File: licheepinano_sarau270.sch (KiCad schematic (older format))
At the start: 0 parts

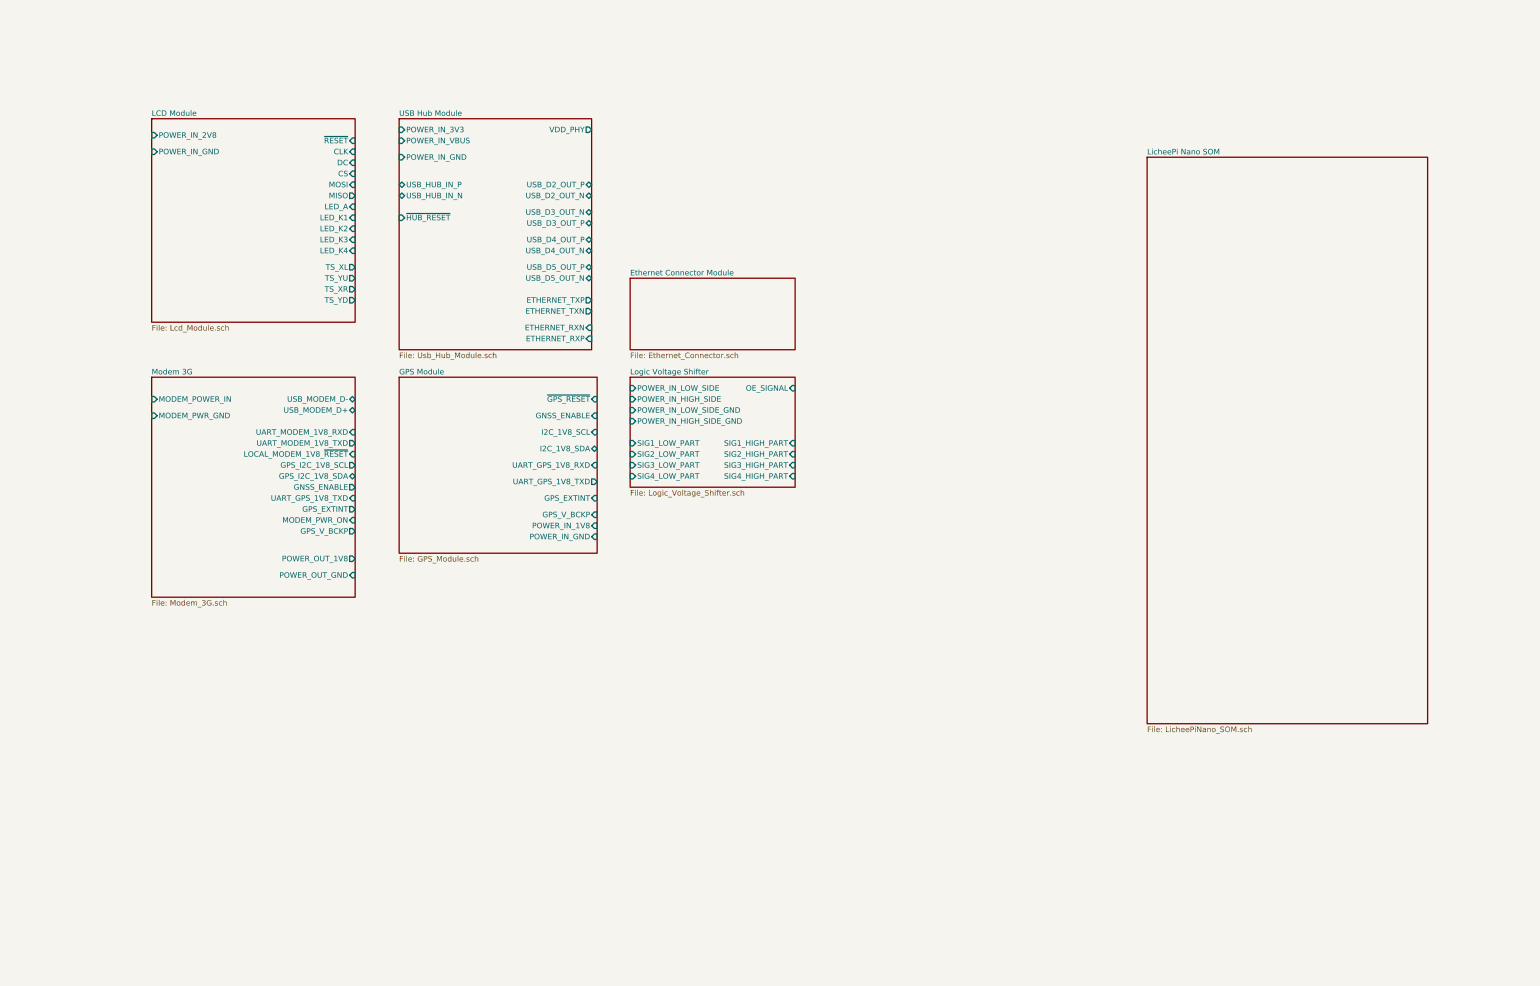
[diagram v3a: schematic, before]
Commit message: Continue connections on schematic
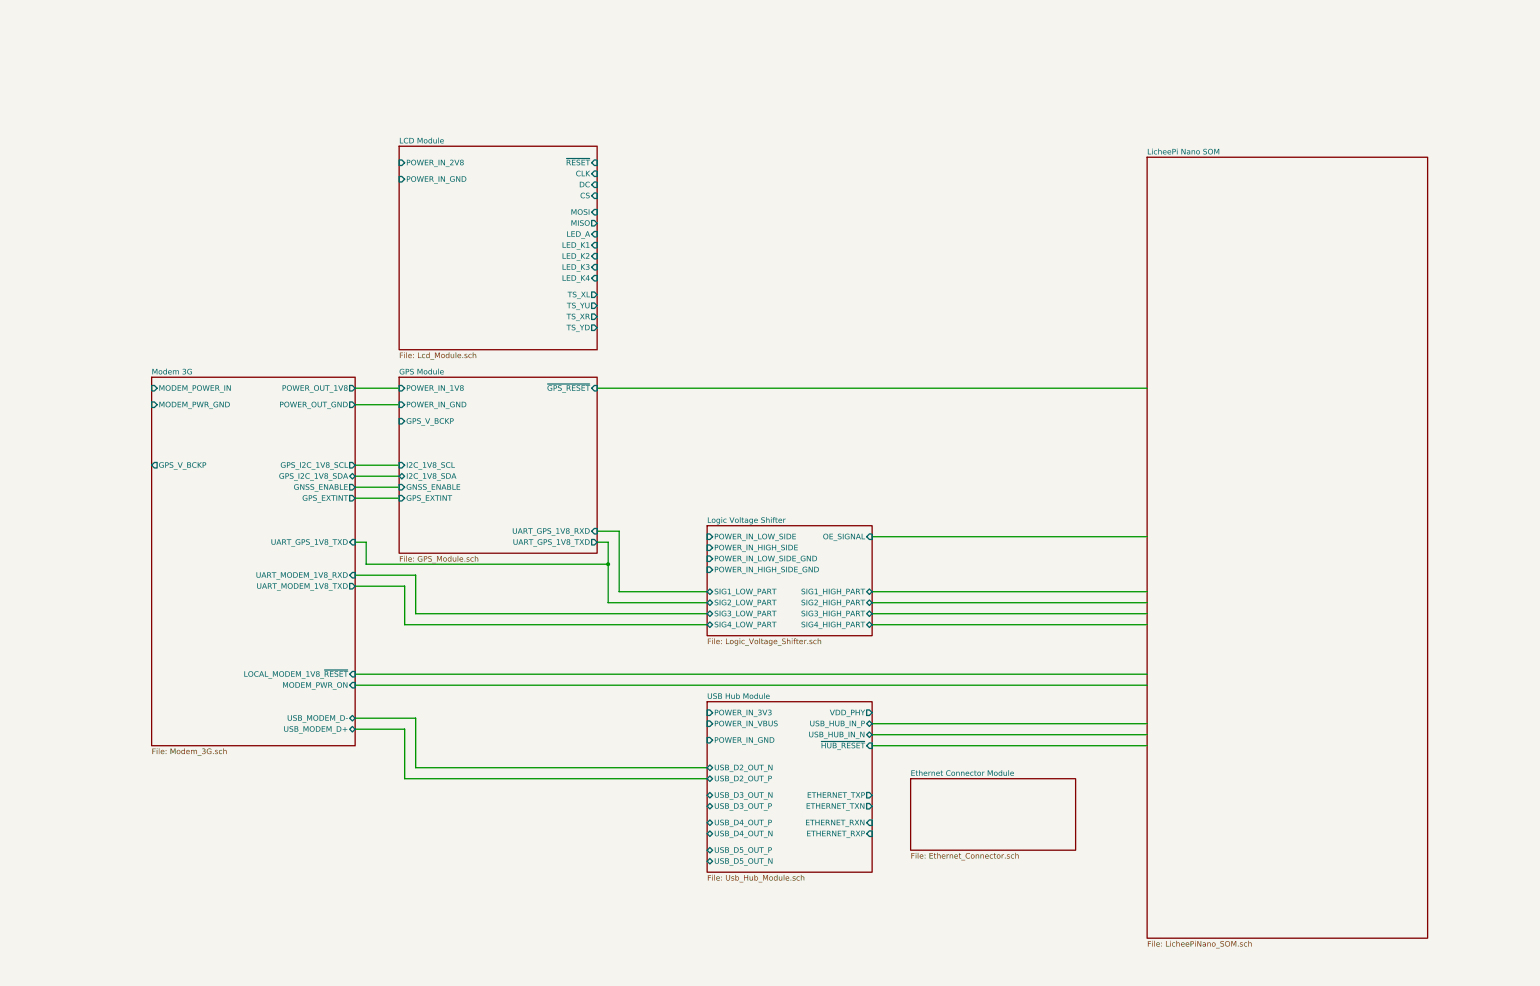
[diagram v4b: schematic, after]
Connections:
- wire segments 0 -> 39
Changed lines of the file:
@@
 $EndDescr
 $Sheet
-S 12050 2250 2550 5150
+S 12050 2250 2550 7100
 U 5FB0031F
 F0 "LicheePi Nano SOM" 50
@@
 $EndSheet
 $Sheet
-S 3000 1900 1850 1850
+S 5250 2150 1800 1850
 U 5FB02458
 F0 "LCD Module" 50
 F1 "Lcd_Module.sch" 50
-F2 "POWER_IN_2V8" I L 3000 2050 50
-F3 "POWER_IN_GND" I L 3000 2200 50
-F4 "~RESET" I R 4850 2100 50
-F5 "CLK" I R 4850 2200 50
-F6 "DC" I R 4850 2300 50
-F7 "CS" I R 4850 2400 50
-F8 "MOSI" I R 4850 2500 50
-F9 "MISO" O R 4850 2600 50
-F10 "LED_A" I R 4850 2700 50
-F11 "LED_K1" I R 4850 2800 50
-F12 "LED_K2" I R 4850 2900 50
-F13 "LED_K3" I R 4850 3000 50
-F14 "LED_K4" I R 4850 3100 50
-F15 "TS_XL" O R 4850 3250 50
-F16 "TS_YU" O R 4850 3350 50
-F17 "TS_XR" O R 4850 3450 50
-F18 "TS_YD" O R 4850 3550 50
+F2 "POWER_IN_2V8" I L 5250 2300 50
+F3 "POWER_IN_GND" I L 5250 2450 50
+F4 "~RESET" I R 7050 2300 50
+F5 "CLK" I R 7050 2400 50
+F6 "DC" I R 7050 2500 50
+F7 "CS" I R 7050 2600 50
+F8 "MOSI" I R 7050 2750 50
+F9 "MISO" O R 7050 2850 50
+F10 "LED_A" I R 7050 2950 50
+F11 "LED_K1" I R 7050 3050 50
+F12 "LED_K2" I R 7050 3150 50
+F13 "LED_K3" I R 7050 3250 50
+F14 "LED_K4" I R 7050 3350 50
+F15 "TS_XL" O R 7050 3500 50
+F16 "TS_YU" O R 7050 3600 50
+F17 "TS_XR" O R 7050 3700 50
+F18 "TS_YD" O R 7050 3800 50
 $EndSheet
 $Sheet
-S 5250 1900 1750 2100
+S 8050 7200 1500 1550
 U 5FB1924B
 F0 "USB Hub Module" 50
 F1 "Usb_Hub_Module.sch" 50
-F2 "USB_HUB_IN_P" B L 5250 2500 50
-F3 "USB_HUB_IN_N" B L 5250 2600 50
-F4 "USB_D5_OUT_N" B R 7000 3350 50
-F5 "USB_D5_OUT_P" B R 7000 3250 50
-F6 "USB_D3_OUT_P" B R 7000 2850 50
-F7 "USB_D3_OUT_N" B R 7000 2750 50
-F8 "USB_D4_OUT_P" B R 7000 3000 50
-F9 "USB_D4_OUT_N" B R 7000 3100 50
-F10 "USB_D2_OUT_P" B R 7000 2500 50
-F11 "USB_D2_OUT_N" B R 7000 2600 50
-F12 "~HUB_RESET" I L 5250 2800 50
-F13 "ETHERNET_TXP" O R 7000 3550 50
-F14 "ETHERNET_TXN" O R 7000 3650 50
-F15 "ETHERNET_RXN" I R 7000 3800 50
-F16 "ETHERNET_RXP" I R 7000 3900 50
-F17 "VDD_PHY" O R 7000 2000 50
-F18 "POWER_IN_3V3" I L 5250 2000 50
-F19 "POWER_IN_VBUS" I L 5250 2100 50
-F20 "POWER_IN_GND" I L 5250 2250 50
+F2 "USB_HUB_IN_P" B R 9550 7400 50
+F3 "USB_HUB_IN_N" B R 9550 7500 50
+F4 "USB_D5_OUT_N" B L 8050 8650 50
+F5 "USB_D5_OUT_P" B L 8050 8550 50
+F6 "USB_D3_OUT_P" B L 8050 8150 50
+F7 "USB_D3_OUT_N" B L 8050 8050 50
+F8 "USB_D4_OUT_P" B L 8050 8300 50
+F9 "USB_D4_OUT_N" B L 8050 8400 50
+F10 "USB_D2_OUT_P" B L 8050 7900 50
+F11 "USB_D2_OUT_N" B L 8050 7800 50
+F12 "~HUB_RESET" I R 9550 7600 50
+F13 "ETHERNET_TXP" O R 9550 8050 50
+F14 "ETHERNET_TXN" O R 9550 8150 50
+F15 "ETHERNET_RXN" I R 9550 8300 50
+F16 "ETHERNET_RXP" I R 9550 8400 50
+F17 "VDD_PHY" O R 9550 7300 50
+F18 "POWER_IN_3V3" I L 8050 7300 50
+F19 "POWER_IN_VBUS" I L 8050 7400 50
+F20 "POWER_IN_GND" I L 8050 7550 50
 $EndSheet
 $Sheet
-S 3000 4250 1850 2000
+S 3000 4250 1850 3350
 U 5FB33D69
 F0 "Modem 3G" 50
 F1 "Modem_3G.sch" 50
-F2 "USB_MODEM_D-" B R 4850 4450 50
-F3 "USB_MODEM_D+" B R 4850 4550 50
-F4 "UART_MODEM_1V8_RXD" I R 4850 4750 50
-F5 "UART_MODEM_1V8_TXD" O R 4850 4850 50
-F6 "LOCAL_MODEM_1V8_~RESET" I R 4850 4950 50
+F2 "USB_MODEM_D-" B R 4850 7350 50
+F3 "USB_MODEM_D+" B R 4850 7450 50
+F4 "UART_MODEM_1V8_RXD" I R 4850 6050 50
+F5 "UART_MODEM_1V8_TXD" O R 4850 6150 50
+F6 "LOCAL_MODEM_1V8_~RESET" I R 4850 6950 50
 F7 "GPS_I2C_1V8_SCL" O R 4850 5050 50
 F8 "GPS_I2C_1V8_SDA" B R 4850 5150 50
 F9 "GNSS_ENABLE" O R 4850 5250 50
-F10 "UART_GPS_1V8_TXD" I R 4850 5350 50
-F11 "GPS_EXTINT" O R 4850 5450 50
-F12 "MODEM_PWR_ON" I R 4850 5550 50
-F13 "GPS_V_BCKP" O R 4850 5650 50
-F14 "MODEM_POWER_IN" I L 3000 4450 50
-F15 "MODEM_PWR_GND" I L 3000 4600 50
-F16 "POWER_OUT_1V8" O R 4850 5900 50
-F17 "POWER_OUT_GND" I R 4850 6050 50
+F10 "UART_GPS_1V8_TXD" I R 4850 5750 50
+F11 "GPS_EXTINT" O R 4850 5350 50
+F12 "MODEM_PWR_ON" I R 4850 7050 50
+F13 "GPS_V_BCKP" O L 3000 5050 50
+F14 "MODEM_POWER_IN" I L 3000 4350 50
+F15 "MODEM_PWR_GND" I L 3000 4500 50
+F16 "POWER_OUT_1V8" O R 4850 4350 50
+F17 "POWER_OUT_GND" O R 4850 4500 50
 $EndSheet
 $Sheet
@@
 F0 "GPS Module" 50
 F1 "GPS_Module.sch" 50
-F2 "~GPS_RESET" I R 7050 4450 50
-F3 "GNSS_ENABLE" I R 7050 4600 50
-F4 "I2C_1V8_SCL" I R 7050 4750 50
-F5 "I2C_1V8_SDA" B R 7050 4900 50
-F6 "UART_GPS_1V8_RXD" I R 7050 5050 50
-F7 "UART_GPS_1V8_TXD" O R 7050 5200 50
-F8 "GPS_EXTINT" I R 7050 5350 50
-F9 "GPS_V_BCKP" I R 7050 5500 50
-F10 "POWER_IN_1V8" I R 7050 5600 50
-F11 "POWER_IN_GND" I R 7050 5700 50
+F2 "~GPS_RESET" I R 7050 4350 50
+F3 "GNSS_ENABLE" I L 5250 5250 50
+F4 "I2C_1V8_SCL" I L 5250 5050 50
+F5 "I2C_1V8_SDA" B L 5250 5150 50
+F6 "UART_GPS_1V8_RXD" I R 7050 5650 50
+F7 "UART_GPS_1V8_TXD" O R 7050 5750 50
+F8 "GPS_EXTINT" I L 5250 5350 50
+F9 "GPS_V_BCKP" I L 5250 4650 50
+F10 "POWER_IN_1V8" I L 5250 4350 50
+F11 "POWER_IN_GND" I L 5250 4500 50
 $EndSheet
 $Sheet
-S 7350 4250 1500 1000
+S 8050 5600 1500 1000
 U 5FC54F14
 F0 "Logic Voltage Shifter" 50
 F1 "Logic_Voltage_Shifter.sch" 50
-F2 "POWER_IN_LOW_SIDE" I L 7350 4350 50
-F3 "POWER_IN_HIGH_SIDE" I L 7350 4450 50
-F4 "POWER_IN_LOW_SIDE_GND" I L 7350 4550 50
-F5 "POWER_IN_HIGH_SIDE_GND" I L 7350 4650 50
-F6 "OE_SIGNAL" I R 8850 4350 50
-F7 "SIG1_LOW_PART" I L 7350 4850 50
-F8 "SIG2_LOW_PART" I L 7350 4950 50
-F9 "SIG3_LOW_PART" I L 7350 5050 50
-F10 "SIG4_LOW_PART" I L 7350 5150 50
-F11 "SIG4_HIGH_PART" I R 8850 5150 50
-F12 "SIG3_HIGH_PART" I R 8850 5050 50
-F13 "SIG2_HIGH_PART" I R 8850 4950 50
-F14 "SIG1_HIGH_PART" I R 8850 4850 50
+F2 "POWER_IN_LOW_SIDE" I L 8050 5700 50
+F3 "POWER_IN_HIGH_SIDE" I L 8050 5800 50
+F4 "POWER_IN_LOW_SIDE_GND" I L 8050 5900 50
+F5 "POWER_IN_HIGH_SIDE_GND" I L 8050 6000 50
+F6 "OE_SIGNAL" I R 9550 5700 50
+F7 "SIG1_LOW_PART" B L 8050 6200 50
+F8 "SIG2_LOW_PART" B L 8050 6300 50
+F9 "SIG3_LOW_PART" B L 8050 6400 50
+F10 "SIG4_LOW_PART" B L 8050 6500 50
+F11 "SIG4_HIGH_PART" B R 9550 6500 50
+F12 "SIG3_HIGH_PART" B R 9550 6400 50
+F13 "SIG2_HIGH_PART" B R 9550 6300 50
+F14 "SIG1_HIGH_PART" B R 9550 6200 50
 $EndSheet
 $Sheet
-S 7350 3350 1500 650
+S 9900 7900 1500 650
 U 5FBCC428
 F0 "Ethernet Connector Module" 50
 F1 "Ethernet_Connector.sch" 50
 $EndSheet
+Wire Wire Line
+	4850 6150 5300 6150
+Wire Wire Line
+	5300 6150 5300 6500
+Wire Wire Line
+	5300 6500 8050 6500
+Wire Wire Line
+	4850 6050 5400 6050
+Wire Wire Line
+	5400 6050 5400 6400
+Wire Wire Line
+	5400 6400 8050 6400
+Wire Wire Line
+	7050 5750 7150 5750
+Wire Wire Line
+	7150 5750 7150 5950
+Wire Wire Line
+	7150 6300 8050 6300
+Wire Wire Line
+	7050 5650 7250 5650
+Wire Wire Line
+	7250 5650 7250 6200
+Wire Wire Line
+	7250 6200 8050 6200
+Wire Wire Line
+	5250 5150 4850 5150
+Wire Wire Line
+	4850 5050 5250 5050
+Wire Wire Line
+	5250 5250 4850 5250
+Wire Wire Line
+	4850 5350 5250 5350
+Wire Wire Line
+	5250 4350 4850 4350
+Wire Wire Line
+	4850 4500 5250 4500
+Wire Wire Line
+	7150 5950 4950 5950
+Wire Wire Line
+	4950 5950 4950 5750
+Wire Wire Line
+	4950 5750 4850 5750
+Connection ~ 7150 5950
+Wire Wire Line
+	7150 5950 7150 6300
+Wire Wire Line
+	7050 4350 12050 4350
+Wire Wire Line
+	4850 6950 12050 6950
+Wire Wire Line
+	4850 7050 12050 7050
+Wire Wire Line
+	8050 7800 5400 7800
+Wire Wire Line
+	5400 7800 5400 7350
+Wire Wire Line
+	5400 7350 4850 7350
+Wire Wire Line
+	4850 7450 5300 7450
+Wire Wire Line
+	5300 7450 5300 7900
+Wire Wire Line
+	5300 7900 8050 7900
+Wire Wire Line
+	9550 7400 12050 7400
+Wire Wire Line
+	9550 7500 12050 7500
+Wire Wire Line
+	9550 7600 12050 7600
+Wire Wire Line
+	9550 6500 12050 6500
+Wire Wire Line
+	9550 6400 12050 6400
+Wire Wire Line
+	9550 6300 12050 6300
+Wire Wire Line
+	9550 6200 12050 6200
+Wire Wire Line
+	9550 5700 12050 5700
 $EndSCHEMATC

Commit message: Added connection for ethernet modules
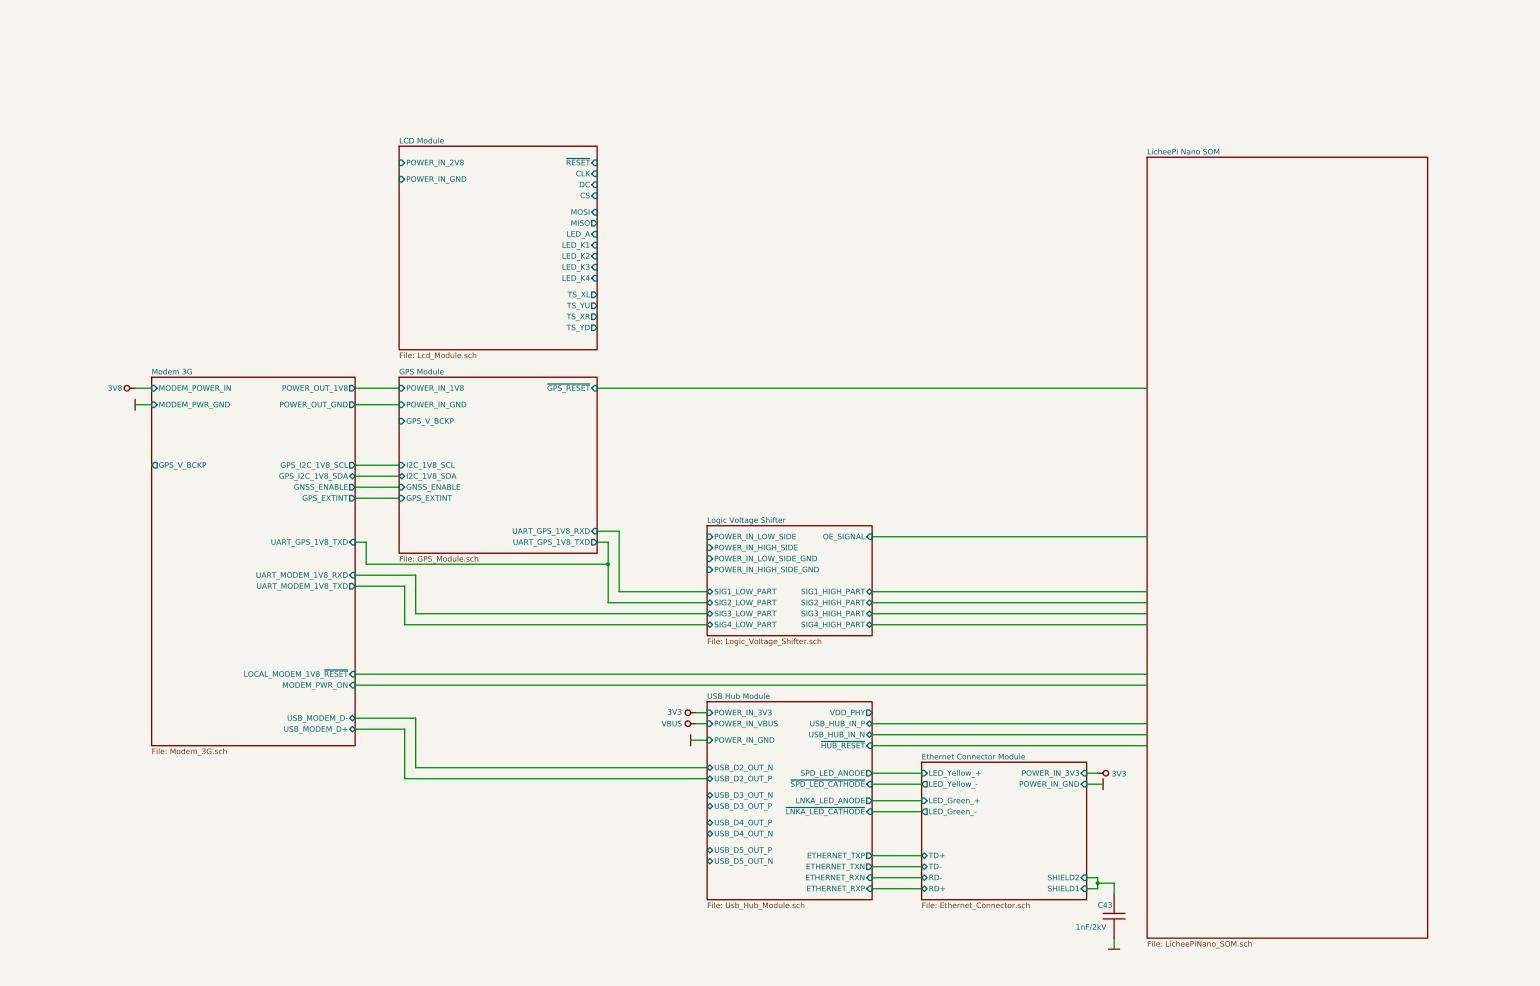
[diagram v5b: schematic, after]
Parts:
- added C43: 1nF/2kV, Capacitors_Smd_1206:1nF_2kV_1206, symbol Capacitors_Smd1206:1nF_2kV_1206
- added Pwr?: 3V8, symbol power:3V8
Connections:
- net labels added: 3V3, GND, VBUS
- wire segments 39 -> 61
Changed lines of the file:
@@
 $EndSheet
 $Sheet
-S 8050 7200 1500 1550
+S 8050 7200 1500 1800
 U 5FB1924B
 F0 "USB Hub Module" 50
@@
 F11 "USB_D2_OUT_N" B L 8050 7800 50
 F12 "~HUB_RESET" I R 9550 7600 50
-F13 "ETHERNET_TXP" O R 9550 8050 50
-F14 "ETHERNET_TXN" O R 9550 8150 50
-F15 "ETHERNET_RXN" I R 9550 8300 50
-F16 "ETHERNET_RXP" I R 9550 8400 50
+F13 "ETHERNET_TXP" O R 9550 8600 50
+F14 "ETHERNET_TXN" O R 9550 8700 50
+F15 "ETHERNET_RXN" I R 9550 8800 50
+F16 "ETHERNET_RXP" I R 9550 8900 50
 F17 "VDD_PHY" O R 9550 7300 50
 F18 "POWER_IN_3V3" I L 8050 7300 50
 F19 "POWER_IN_VBUS" I L 8050 7400 50
 F20 "POWER_IN_GND" I L 8050 7550 50
+F21 "~LNKA_LED_CATHODE" I R 9550 8200 50
+F22 "~SPD_LED_CATHODE" I R 9550 7950 50
+F23 "LNKA_LED_ANODE" O R 9550 8100 50
+F24 "SPD_LED_ANODE" O R 9550 7850 50
 $EndSheet
 $Sheet
@@
 $EndSheet
 $Sheet
-S 9900 7900 1500 650
+S 10000 7750 1500 1250
 U 5FBCC428
 F0 "Ethernet Connector Module" 50
 F1 "Ethernet_Connector.sch" 50
+F2 "TD+" B L 10000 8600 50
+F3 "TD-" B L 10000 8700 50
+F4 "RD+" B L 10000 8900 50
+F5 "RD-" B L 10000 8800 50
+F6 "SHIELD1" I R 11500 8900 50
+F7 "SHIELD2" I R 11500 8800 50
+F8 "LED_Yellow_+" I L 10000 7850 50
+F9 "LED_Yellow_-" O L 10000 7950 50
+F10 "LED_Green_+" I L 10000 8100 50
+F11 "LED_Green_-" O L 10000 8200 50
+F12 "POWER_IN_3V3" I R 11500 7850 50
+F13 "POWER_IN_GND" I R 11500 7950 50
 $EndSheet
 Wire Wire Line
@@
 Wire Wire Line
 	9550 5700 12050 5700
+Wire Wire Line
+	10000 8900 9550 8900
+Wire Wire Line
+	9550 8800 10000 8800
+Wire Wire Line
+	10000 8700 9550 8700
+Wire Wire Line
+	9550 8600 10000 8600
+Wire Wire Line
+	10000 8200 9550 8200
+Wire Wire Line
+	10000 7950 9550 7950
+Wire Wire Line
+	10000 7850 9550 7850
+Wire Wire Line
+	9550 8100 10000 8100
+Wire Wire Line
+	11500 8800 11600 8800
+Wire Wire Line
+	11600 8800 11600 8850
+Wire Wire Line
+	11600 8900 11500 8900
+$Comp
+L Capacitors_Smd1206:1nF_2kV_1206 C43
+U 1 1 5FC74DED
+P 11750 9150
+F 0 "C43" H 11600 9250 50  0000 L CNN
+F 1 "1nF/2kV" H 11400 9050 50  0000 L CNN
+F 2 "Capacitors_Smd_1206:1nF_2kV_1206" H 11550 9250 50  0001 C CNN
+F 3 "Capacitors/Smd_1206/Components_Documentation/1nF_2kV_1206.pdf" H 11550 9250 50  0001 C CNN
+F 4 "YAGEO" H 11750 9150 50  0001 C CNN "Manufacturer"
+F 5 "CC1206KKX7RDBB102" H 11750 9150 50  0001 C CNN "Manufacturer Part Number"
+F 6 "TME" H 11750 9150 50  0001 C CNN "Supplier"
+F 7 "CC1206KKX7RD102" H 11750 9150 50  0001 C CNN "Supplier Part Number"
+F 8 "https://www.tme.eu/pl/details/cc1206kkx7rd102/kondensatory-mlcc-smd-1206/yageo/cc1206kkx7rdbb102/" H 11750 9150 50  0001 C CNN "URL"
+F 9 "0,70900" H 11750 9150 50  0001 C CNN "Price@1pc"
+F 10 "0,15913" H 11750 9150 50  0001 C CNN "Price@1000pcs"
+F 11 "WP" H 11750 9150 50  0001 C CNN "Developer"
+F 12 "1206" H 11750 9150 50  0001 C CNN "Package"
+	1    11750 9150
+	1    0    0    -1
+$EndComp
+Wire Wire Line
+	11600 8850 11750 8850
+Wire Wire Line
+	11750 8850 11750 8950
+Connection ~ 11600 8850
+Wire Wire Line
+	11600 8850 11600 8900
+$Comp
+L power:GND #PWR0147
+U 1 1 5FC78647
+P 11750 9450
+F 0 "#PWR0147" H 11750 9550 30  0001 C CNN
+F 1 "GND" H 11750 9350 30  0001 C CNN
+F 2 "" H 11750 9450 60  0000 C CNN
+F 3 "" H 11750 9450 60  0000 C CNN
+	1    11750 9450
+	1    0    0    -1
+$EndComp
+Wire Wire Line
+	11750 9350 11750 9450
+$Comp
+L power:3V3 #PWR?
+U 1 1 5FCFF763
+P 11600 7850
+F 0 "#PWR?" H 11600 7950 40  0001 C CNN
+F 1 "3V3" V 11606 7978 50  0000 L CNN
+F 2 "" H 11600 7850 60  0000 C CNN
+F 3 "" H 11600 7850 60  0000 C CNN
+	1    11600 7850
+	0    1    1    0
+$EndComp
+$Comp
+L power:GND #PWR?
+U 1 1 5FD0031A
+P 11650 7950
+F 0 "#PWR?" H 11650 8050 30  0001 C CNN
+F 1 "GND" H 11650 7850 30  0001 C CNN
+F 2 "" H 11650 7950 60  0000 C CNN
+F 3 "" H 11650 7950 60  0000 C CNN
+	1    11650 7950
+	0    1    1    0
+$EndComp
+Wire Wire Line
+	11600 7850 11500 7850
+Wire Wire Line
+	11650 7950 11500 7950
+$Comp
+L power:3V3 #PWR?
+U 1 1 5FD02FB7
+P 7950 7300
+F 0 "#PWR?" H 7950 7400 40  0001 C CNN
+F 1 "3V3" V 7956 7428 50  0000 L CNN
+F 2 "" H 7950 7300 60  0000 C CNN
+F 3 "" H 7950 7300 60  0000 C CNN
+	1    7950 7300
+	0    -1   -1   0
+$EndComp
+$Comp
+L power:GND #PWR?
+U 1 1 5FD03003
+P 7900 7550
+F 0 "#PWR?" H 7900 7650 30  0001 C CNN
+F 1 "GND" H 7900 7450 30  0001 C CNN
+F 2 "" H 7900 7550 60  0000 C CNN
+F 3 "" H 7900 7550 60  0000 C CNN
+	1    7900 7550
+	0    -1   -1   0
+$EndComp
+Wire Wire Line
+	7950 7300 8050 7300
+Wire Wire Line
+	7900 7550 8050 7550
+$Comp
+L power:VBUS #PWR?
+U 1 1 5FD086B3
+P 7950 7400
+F 0 "#PWR?" H 7950 7550 30  0001 C CNN
+F 1 "VBUS" V 7949 7527 50  0000 L CNN
+F 2 "" H 7950 7400 50  0001 C CNN
+F 3 "" H 7950 7400 50  0001 C CNN
+	1    7950 7400
+	0    -1   -1   0
+$EndComp
+Wire Wire Line
+	8050 7400 7950 7400
+$Comp
+L power:3V8 Pwr?
+U 1 1 5FD0B699
+P 2850 4350
+F 0 "Pwr?" H 2850 4550 30  0001 C CNN
+F 1 "3V8" V 2850 4600 50  0000 R CNN
+F 2 "" H 2850 4350 50  0001 C CNN
+F 3 "" H 2850 4350 50  0001 C CNN
+	1    2850 4350
+	0    -1   -1   0
+$EndComp
+Wire Wire Line
+	3000 4350 2850 4350
+$Comp
+L power:GND #PWR?
+U 1 1 5FD0E0BF
+P 2850 4500
+F 0 "#PWR?" H 2850 4600 30  0001 C CNN
+F 1 "GND" H 2850 4400 30  0001 C CNN
+F 2 "" H 2850 4500 60  0000 C CNN
+F 3 "" H 2850 4500 60  0000 C CNN
+	1    2850 4500
+	0    -1   -1   0
+$EndComp
+Wire Wire Line
+	2850 4500 3000 4500
 $EndSCHEMATC
